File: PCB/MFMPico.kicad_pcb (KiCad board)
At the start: 2 copper layers, 105 x 102.6 mm, 39 parts, among them J1 ECON34, J2 Conn_02x04_Odd_Even, J3 Micro_SD_Card, J4 Conn_01x16, J5 Conn_01x04, J6 Conn_01x02, J7 Conn_01x02, J8 Conn_01x02, J9 Conn_01x04, P1 CON20, Q1 BC547, SW1 SW_Push, U2 74LS03, U3 74LS03, U4 74LS03, U5 SN65HVD33DR, U6 74LS03

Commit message: Step not a pio program anymore, validated with mfm emulator.
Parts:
- removed Q1: BC547, Package_TO_SOT_THT:TO-92_Inline
- removed R12: 5.1K, Resistor_THT:R_Axial_DIN0207_L6.3mm_D2.5mm_P10.16mm_Horizontal
- J7: value Conn_01x02 -> DNP
- J8: value Conn_01x02 -> PLACE
- R4: value 100R -> DNP
- moved J9 0.30 mm to (178.2, 143.0)
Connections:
- A1 pad 29: unconnected-(A1-GPIO22-Pad29)_1 -> /DRIVE_SEL
- U6 pad 10: unconnected-(U6-Pad10) -> /~DRIVE_SEL
- U6 pad 8: unconnected-(U6-Pad8) -> /DRIVE_SEL
- U6 pad 9: unconnected-(U6-Pad9) -> /~DRIVE_SEL
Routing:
- net /DRIVE_SEL: track 148.4 -> 210.7 mm, vias 4 -> 6
- net GND: track 2.18 -> 15.4 mm
- net /~DRIVE_SEL: track 49.8 -> 60.6 mm
- net Net-(Q1-B): track 5.22 -> 0.00 mm
- net Net-(J9-Pin_2): track 17.0 -> 21.1 mm, vias 0 -> 1
- net /WRITE_GATE: track 140.4 -> 144.1 mm, vias 4 -> 6
- net Net-(J1-Track_0): track 70.0 -> 69.3 mm
- net Net-(J9-Pin_3): track 15.3 -> 15.4 mm, vias 0 -> 1

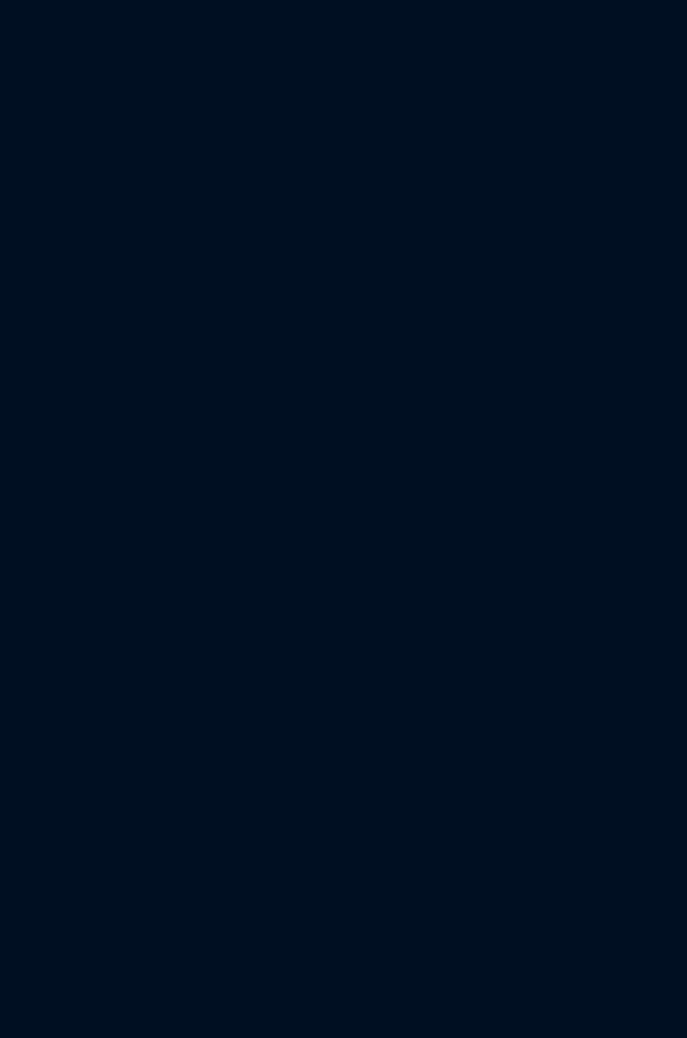
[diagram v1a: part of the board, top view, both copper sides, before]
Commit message: moving to nor gates for drive sel slowly
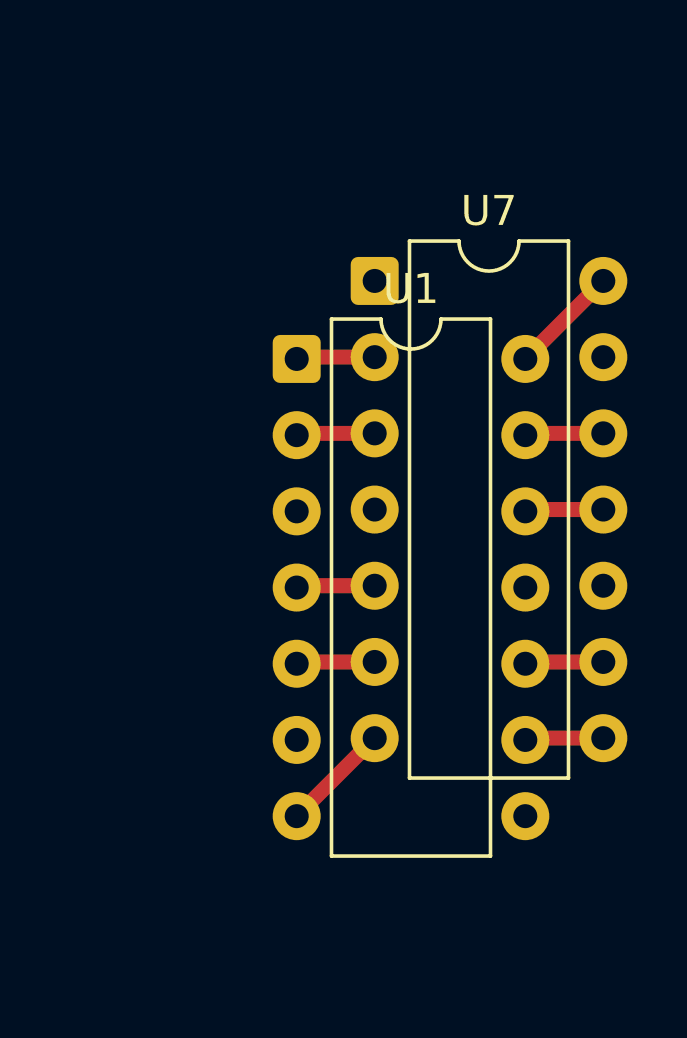
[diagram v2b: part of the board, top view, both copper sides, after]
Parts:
- added U1: 74LS03, Package_DIP:DIP-14_W7.62mm, F.Cu at (243.0, 121.4)
- added U7: 74HC02, Package_DIP:DIP-14_W7.62mm, F.Cu at (245.6, 118.8)
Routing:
- net Net-(U1E-GND): track 0.00 -> 3.68 mm
- net Net-(U1E-VCC): track 0.00 -> 3.68 mm
- net Net-(U1-Pad5): track 0.00 -> 2.62 mm
- net Net-(U1-Pad4): track 0.00 -> 2.62 mm
- net Net-(U1-Pad2): track 0.00 -> 2.62 mm
- net Net-(U1-Pad1): track 0.00 -> 2.62 mm
- net Net-(U1-Pad9): track 0.00 -> 2.62 mm
- net Net-(U1-Pad13): track 0.00 -> 2.62 mm
- net Net-(U1-Pad12): track 0.00 -> 2.62 mm
- net Net-(U1-Pad10): track 0.00 -> 2.62 mm

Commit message: wip on  nor gate version
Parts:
- removed C3: 100n, Capacitor_THT:C_Disc_D3.4mm_W2.1mm_P2.50mm
- removed R13: 220R, Resistor_THT:R_Axial_DIN0207_L6.3mm_D2.5mm_P10.16mm_Horizontal
- removed RN2: R_Network09, Resistor_THT:R_Array_SIP10
- removed U2: 74LS03, Package_DIP:DIP-14_W7.62mm
- added C7: 100n, Capacitor_SMD:C_0603_1608Metric_Pad1.08x0.95mm_HandSolder, F.Cu at (166.6, 134.9)
- added C8: 100n, Capacitor_SMD:C_0603_1608Metric_Pad1.08x0.95mm_HandSolder, F.Cu at (172.8, 134.8)
- added C9: 100n, Capacitor_SMD:C_0603_1608Metric_Pad1.08x0.95mm_HandSolder, F.Cu at (174.8, 127.6)
- added JP1: SolderJumper_2_Open, Jumper:SolderJumper-2_P1.3mm_Open_Pad1.0x1.5mm, F.Cu at (106.6, 75.2)
- added JP2: SolderJumper_2_Open, Jumper:SolderJumper-2_P1.3mm_Open_Pad1.0x1.5mm, F.Cu at (109.2, 75.2)
- added JP3: SolderJumper_2_Open, Jumper:SolderJumper-2_P1.3mm_Open_Pad1.0x1.5mm, F.Cu at (111.8, 75.2)
- added JP4: SolderJumper_2_Open, Jumper:SolderJumper-2_P1.3mm_Open_Pad1.0x1.5mm, F.Cu at (114.4, 75.2)
- added JP5: SolderJumper_2_Open, Jumper:SolderJumper-2_P1.3mm_Open_Pad1.0x1.5mm, F.Cu at (117.0, 75.2)
- added JP6: SolderJumper_2_Open, Jumper:SolderJumper-2_P1.3mm_Open_Pad1.0x1.5mm, F.Cu at (119.6, 75.2)
- added JP7: SolderJumper_2_Open, Jumper:SolderJumper-2_P1.3mm_Open_Pad1.0x1.5mm, F.Cu at (124.8, 75.2)
- added JP8: SolderJumper_2_Open, Jumper:SolderJumper-2_P1.3mm_Open_Pad1.0x1.5mm, F.Cu at (122.2, 75.2)
- added R10: 1K, Resistor_SMD:R_0603_1608Metric, F.Cu at (131.4, 107.8)
- added R11: 1K, Resistor_SMD:R_0603_1608Metric, F.Cu at (131.4, 105.2)
- added R5: 1K, Resistor_SMD:R_0603_1608Metric, F.Cu at (131.4, 138.4)
- added R6: 1K, Resistor_SMD:R_0603_1608Metric, F.Cu at (131.4, 133.2)
- added R7: 1K, Resistor_SMD:R_0603_1608Metric, F.Cu at (131.4, 115.3)
- added R8: 1K, Resistor_SMD:R_0603_1608Metric, F.Cu at (131.4, 112.8)
- added R9: 1K, Resistor_SMD:R_0603_1608Metric, F.Cu at (131.4, 110.3)
- added U8: SN74LVC1G00DBV, Package_TO_SOT_SMD:SOT-23-5_HandSoldering, F.Cu at (172.0, 127.5)
- C1, C2, C4, C5, C6: footprint Capacitor_THT:C_Disc_D3.4mm_W2.1mm_P2.50mm -> Capacitor_SMD:C_0603_1608Metric_Pad1.08x0.95mm_HandSolder
- J3: value Micro_SD_Card -> Micro_SD_Card_Det1
- U1: value 74LS03 -> 74LVC1G02; footprint Package_DIP:DIP-14_W7.62mm -> Package_TO_SOT_SMD:SOT-23-5_HandSoldering
- U3, U4: value 74LS03 -> 74LS33
- U6: value 74LS03 -> 74LS05
- U7: value 74HC02 -> SN74LVC1G00DBV; footprint Package_DIP:DIP-14_W7.62mm -> Package_TO_SOT_SMD:SOT-23-5_HandSoldering
- moved U1 80.0 mm to (163.8, 132.7), turned to -90 degrees
- moved U7 76.8 mm to (170.0, 132.5), turned to -90 degrees
- moved J3 69.1 mm to (110.1, 56.9), turned to 180 degrees
- moved C1 61.7 mm to (106.0, 58.8), turned to -90 degrees
- moved C6 42.5 mm to (166.8, 79.1)
- moved RN1 35.0 mm to (140.4, 73.8), turned to 0 degrees
- moved J4 31.4 mm to (127.8, 140.7)
- moved A1 31.0 mm to (110.7, 125.9)
- moved D1 31.0 mm to (96.0, 146.0)
- moved U6 29.0 mm to (139.4, 117.0)
- moved C2 28.3 mm to (148.0, 114.2)
- moved SW1 23.2 mm to (90.0, 120.0)
- moved U4 23.0 mm to (156.8, 79.9), turned to 0 degrees
- moved C4 15.0 mm to (149.8, 79.0), turned to 90 degrees
- moved J8 12.3 mm to (164.2, 138.6), turned to 0 degrees
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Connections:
- A1 pad 22: unconnected-(A1-GPIO17-Pad22) -> /SCLK
- A1 pad 24: /SCLK -> Net-(A1-GPIO18)
- A1 pad 25: /MOSI -> Net-(A1-GPIO19)
- A1 pad 26: /MISO -> Net-(A1-GPIO20)
- A1 pad 27: /CS -> Net-(A1-GPIO21)
- A1 pad 29: /DRIVE_SEL -> /CS/D3
- J3 pad 1: unconnected-(J3-DAT2-Pad1) -> /D2
- J3 pad 2: /CS -> /CS/D3
- J3 pad 7: /MISO -> /MISO/D0
- J3 pad 8: unconnected-(J3-DAT1-Pad8) -> /D1
- J3 pad 9: GND -> unconnected-(J3-DET-Pad9)
- U1 pad 1: Net-(U1-Pad1) -> /~WRITE_GATE
- U1 pad 2: Net-(U1-Pad2) -> /~DRIVE_SEL
- U1 pad 3: Net-(U1-Pad3) -> GND
- U1 pad 4: Net-(U1-Pad4) -> Net-(J7-Pin_1)
- U1 pad 5: Net-(U1-Pad5) -> +3.3V
- U3 pad 1: /DRIVE_SEL -> /HEAD_3
- U3 pad 10: /WRITE_FAULT -> /DIR_IN
- U3 pad 11: Net-(J1-Track_0) -> /~DRIVE_SEL
- U3 pad 12: /DRIVE_SEL -> Net-(J1-Head_0)
- U3 pad 13: /TRACK_0 -> /HEAD_0
- U3 pad 2: Net-(J1-Head_1) -> /~DRIVE_SEL
- U3 pad 3: /HEAD_1 -> Net-(J1-Head_3/REDWR)
- U3 pad 4: /DRIVE_SEL -> /HEAD_2
- U3 pad 5: Net-(J1-Head_0) -> /~DRIVE_SEL
- U3 pad 6: /HEAD_0 -> Net-(J1-Head_2)
- U3 pad 8: Net-(J1-Write_Fault) -> /~DRIVE_SEL
- U3 pad 9: /DRIVE_SEL -> Net-(J1-Direction_In)
- U4 pad 1: /DRIVE_SEL -> /HEAD_1
- U4 pad 10: Net-(J1-Head_2) -> /WRITE_GATE
- U4 pad 11: /DIR_IN -> (no net)
- U4 pad 12: /DRIVE_SEL -> (no net)
- U4 pad 13: Net-(J1-Direction_In) -> (no net)
- U4 pad 2: /SEEK_COMPL -> /~DRIVE_SEL
- U4 pad 3: Net-(J1-Seek_Complete) -> Net-(J1-Head_1)
- U4 pad 4: /DRIVE_SEL -> /STEP
- U4 pad 5: /~WRITE_GATE -> /~DRIVE_SEL
- U4 pad 6: /WRITE_GATE -> Net-(J1-Step)
- U4 pad 8: /HEAD_2 -> /~DRIVE_SEL
- U4 pad 9: /DRIVE_SEL -> /~WRITE_GATE
- U6 pad 1: Net-(J7-Pin_1) -> /SEEK_COMPL
- U6 pad 10: /~DRIVE_SEL -> Net-(J1-Ready)
- U6 pad 11: unconnected-(U6-Pad11) -> /READY
- U6 pad 2: /DRIVE_SEL -> Net-(J1-Seek_Complete)
- U6 pad 3: Net-(J8-Pin_1) -> /TRACK_0
- U6 pad 4: /~WRITE_GATE -> Net-(J1-Track_0)
- U6 pad 5: /DRIVE_SEL -> /WRITE_FAULT
- U6 pad 6: Net-(J7-Pin_1) -> Net-(J1-Write_Fault)
- U6 pad 8: /DRIVE_SEL -> Net-(J1-Index)
- U6 pad 9: /~DRIVE_SEL -> /INDEX
- U7 pad 1: Net-(U1-Pad3) -> Net-(U7-Pad1)
- U7 pad 2: Net-(U1-Pad1) -> /~WRITE_GATE
- U7 pad 3: Net-(U1-Pad2) -> GND
- U7 pad 4: Net-(U1-Pad6) -> Net-(J8-Pin_1)
- U7 pad 5: Net-(U1-Pad4) -> +3.3V
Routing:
- net GND: track 15.4 -> 597.2 mm, vias 14 -> 16
- net /DRIVE_SEL: track 210.7 -> 0.00 mm, vias 6 -> 0
- net +3.3V: track 130.5 -> 276.9 mm, vias 2 -> 13
- net /CS/D3: track 0.00 -> 99.5 mm, vias 0 -> 3
- net /WRITE_FAULT: track 102.3 -> 20.4 mm, vias 3 -> 0
- net +5V: track 271.4 -> 200.6 mm, vias 0 -> 1
- net /~DRIVE_SEL: track 60.6 -> 131.3 mm, vias 1 -> 3
- net Net-(A1-GPIO21): track 0.00 -> 57.3 mm
- net /WRITE_GATE: track 144.1 -> 87.0 mm, vias 6 -> 4
- net /TRACK_0: track 75.4 -> 20.4 mm, vias 2 -> 0
- net Net-(A1-GPIO20): track 0.00 -> 47.5 mm, vias 0 -> 1
- net /CS: track 46.7 -> 0.00 mm, vias 1 -> 0
- net /MISO: track 44.8 -> 0.00 mm, vias 1 -> 0
- net Net-(J1-Step): track 27.8 -> 72.4 mm
- net Net-(A1-GPIO18): track 0.00 -> 44.4 mm
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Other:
- outline, holes or cut-outs redrawn
- board text added: "LED/ clicker"
- board text removed: "LED/clicker"

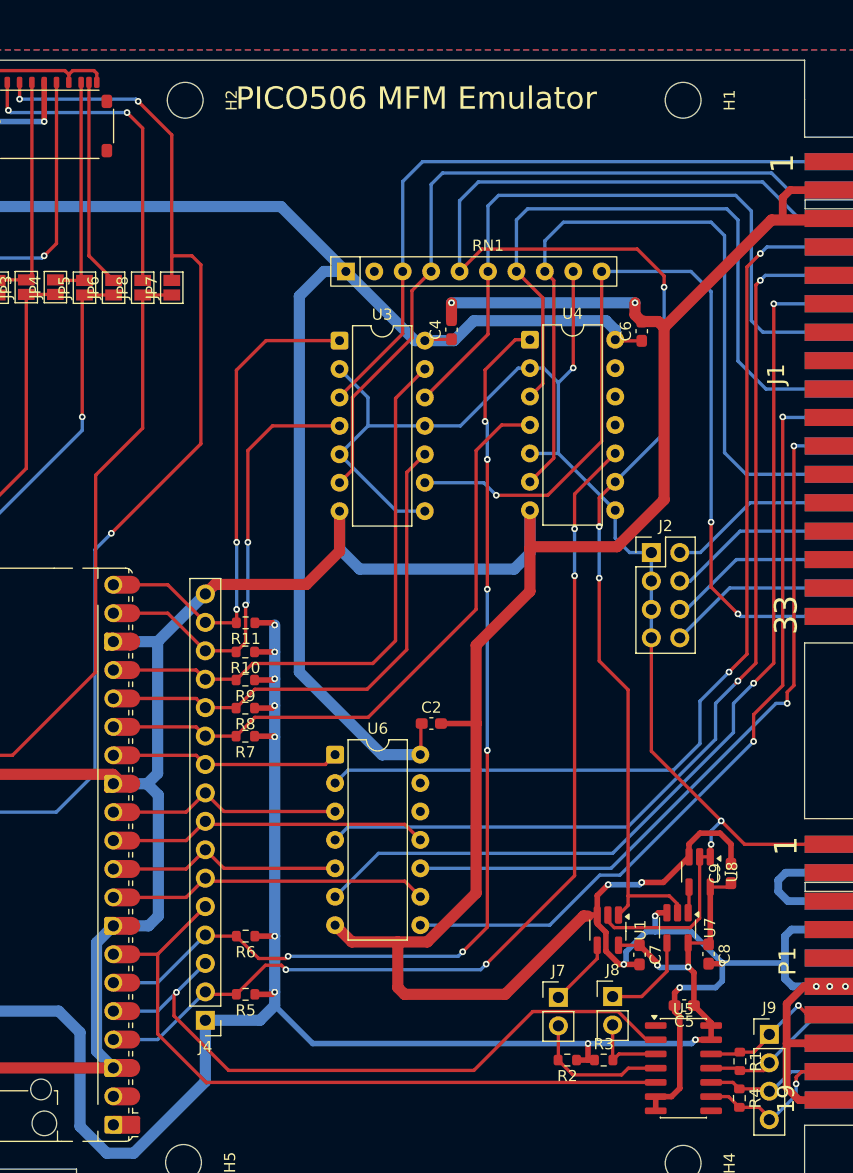
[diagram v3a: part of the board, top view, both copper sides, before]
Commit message: New PCB works, apart from an odd low level format issue
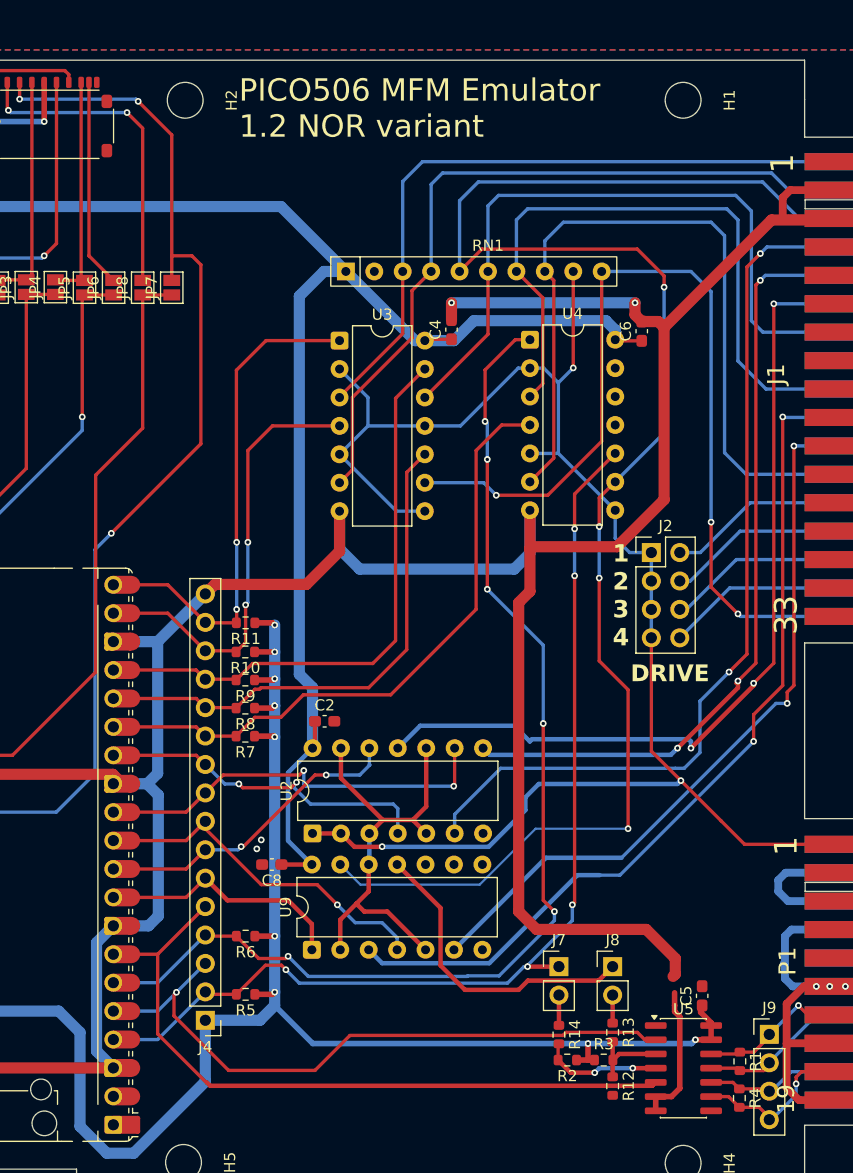
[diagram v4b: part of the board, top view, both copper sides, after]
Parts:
- removed C7, C9: 100n, Capacitor_SMD:C_0603_1608Metric_Pad1.08x0.95mm_HandSolder
- removed U1: 74LVC1G02, Package_TO_SOT_SMD:SOT-23-5_HandSoldering
- removed U6: 74LS05, Package_DIP:DIP-14_W7.62mm
- removed U7, U8: SN74LVC1G00DBV, Package_TO_SOT_SMD:SOT-23-5_HandSoldering
- added R12: DNP, Resistor_SMD:R_0603_1608Metric, F.Cu at (164.2, 146.6)
- added R13: 100R, Resistor_SMD:R_0603_1608Metric, F.Cu at (164.2, 141.8)
- added R14: 100R, Resistor_SMD:R_0603_1608Metric, F.Cu at (159.4, 142.0)
- added U2: 74LS03, Package_DIP:DIP-14_W7.62mm, F.Cu at (137.4, 124.0)
- added U9: 74LS03, Package_DIP:DIP-14_W7.62mm, F.Cu at (137.3, 134.4)
- moved C8 39.8 mm to (133.7, 126.8), turned to 180 degrees
- moved C2 9.54 mm to (138.5, 114.0)
- moved J7 2.75 mm to (159.4, 135.9)
- moved J8 2.67 mm to (164.2, 135.9)
- moved C5 1.82 mm to (172.2, 138.5), turned to 90 degrees
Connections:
- C8 pad 1: +3.3V -> +5V
- J7 pad 1: Net-(J7-Pin_1) -> /WRITE_GATE
- R2 pad 2: Net-(J7-Pin_2) -> Net-(U5-DE)
- R3 pad 2: Net-(J8-Pin_2) -> Net-(U5-RE)
- U5 pad 3: Net-(J8-Pin_2) -> Net-(U5-RE)
- U5 pad 4: Net-(J7-Pin_2) -> Net-(U5-DE)
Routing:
- net GND: track 597.2 -> 515.0 mm, vias 16 -> 12
- net /DRIVE_SEL: track 0.00 -> 40.4 mm
- net +3.3V: track 276.9 -> 254.6 mm, vias 13 -> 11
- net Net-(J8-Pin_1): track 8.43 -> 27.8 mm
- net Net-(J1-Track_0): track 89.6 -> 72.2 mm, vias 2 -> 3
- net /~DRIVE_SEL: track 131.3 -> 148.5 mm
- net /TRACK_0: track 20.4 -> 35.9 mm, vias 0 -> 2
- net /~WRITE_GATE: track 130.8 -> 145.8 mm, vias 3 -> 4
- net Net-(U5-DE): track 0.00 -> 10.9 mm, vias 0 -> 2
- net Net-(J1-Write_Fault): track 89.3 -> 79.0 mm, vias 2 -> 3
- net /SEEK_COMPL: track 19.7 -> 29.8 mm, vias 0 -> 2
- net Net-(J7-Pin_2): track 12.6 -> 2.71 mm
- net /HEAD_1: track 92.2 -> 101.9 mm
- net +5V: track 200.6 -> 208.6 mm
- net Net-(J1-Seek_Complete): track 89.4 -> 82.0 mm
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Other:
- board text added: "1 2 3 4"
- board text added: "DRIVE"
- board text added: "PICO506 MFM Emulator 1.2 NOR variant"
- board text removed: "PICO506 MFM Emulator"
